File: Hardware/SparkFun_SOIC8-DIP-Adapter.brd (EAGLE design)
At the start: 20.8 x 20.8 mm, 17 parts, among them U1 GENERIC-SOIC8, U2 GENERIC-SOIC8, U3 GENERIC-SOIC8, U4 GENERIC-SOIC8

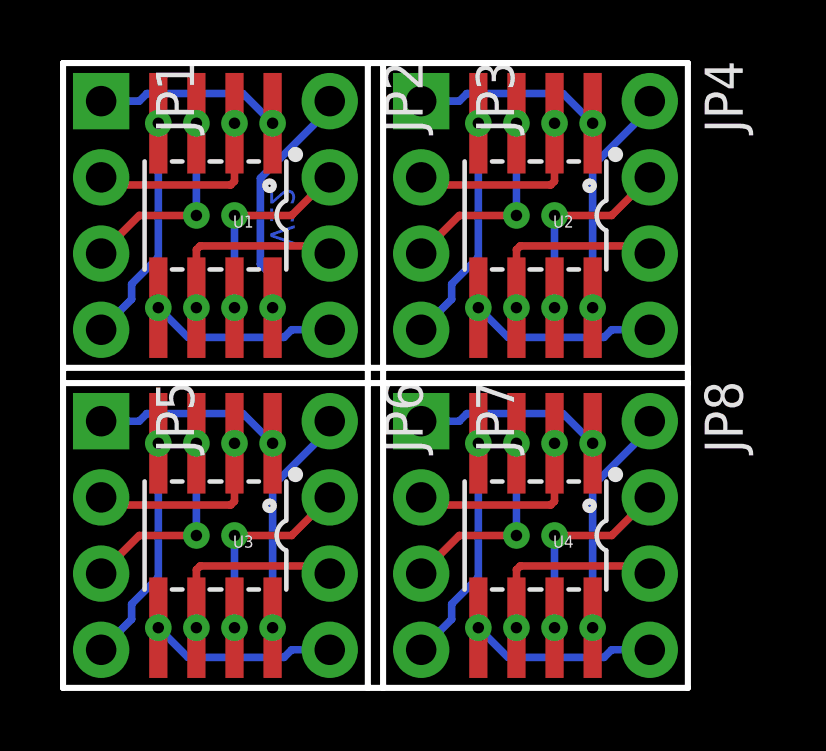
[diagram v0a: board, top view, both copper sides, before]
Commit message: Moving version numbers back to V11, matching branch name.
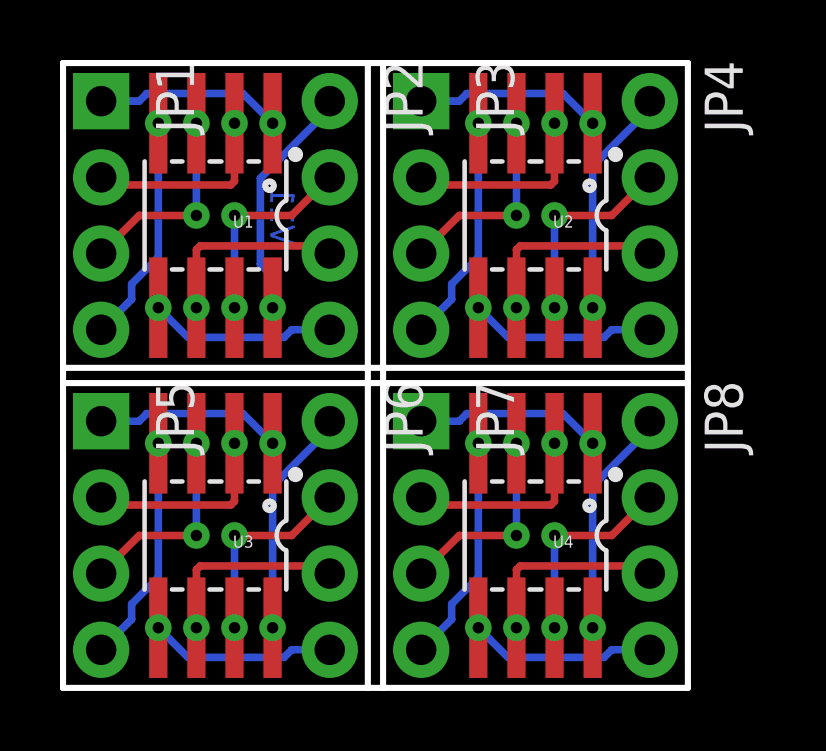
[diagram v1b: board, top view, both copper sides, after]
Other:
- board text added: "V11"
- board text removed: "V12"
